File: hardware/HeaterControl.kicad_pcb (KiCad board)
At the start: 2 copper layers, 31.5 x 27.2 mm, 17 parts, among them J1 UART, J2 BTN, J3 OLED, P1 TC2030-CTX, Q1 NX7002AK.215, Q2 NX7002AK.215, SW1 RESET, U1 DS18B20, U2 BL654, U3 SHT30-DIS-B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

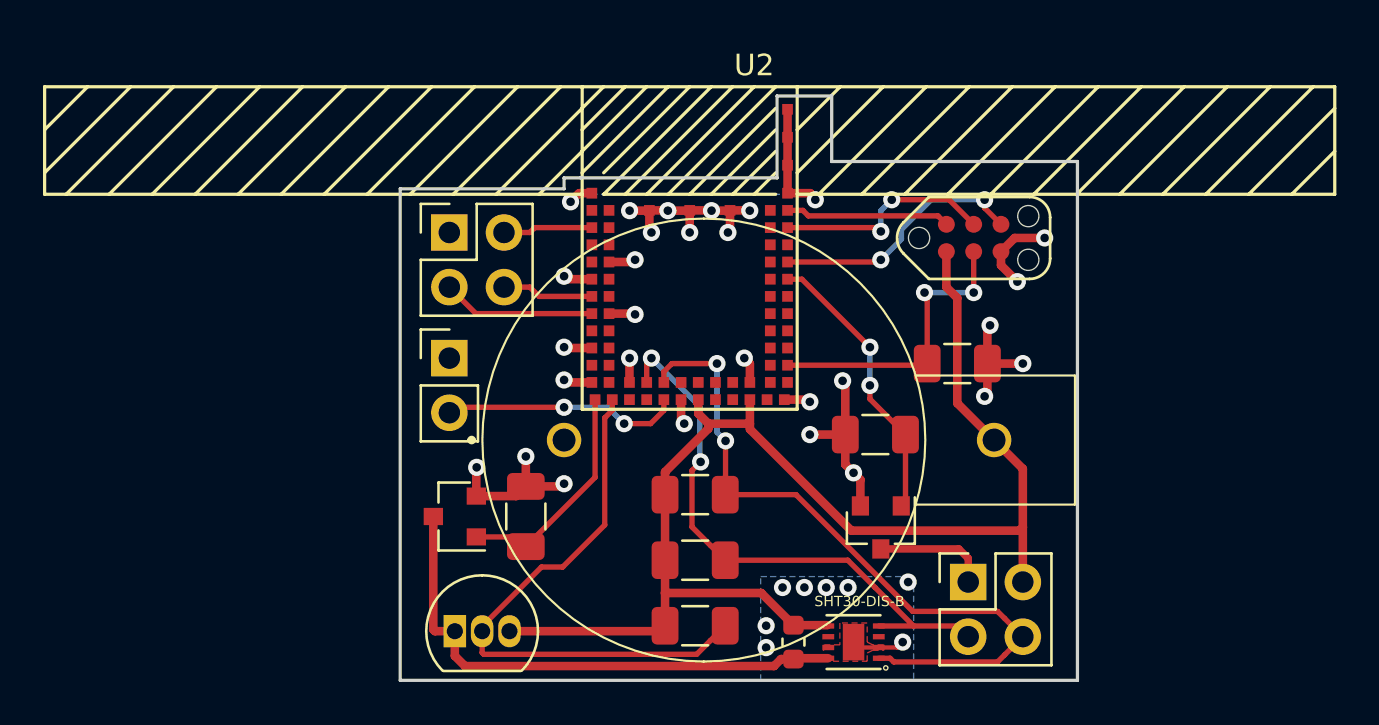
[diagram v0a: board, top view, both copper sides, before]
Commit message: Removed Sensor/Oled PWR circuts
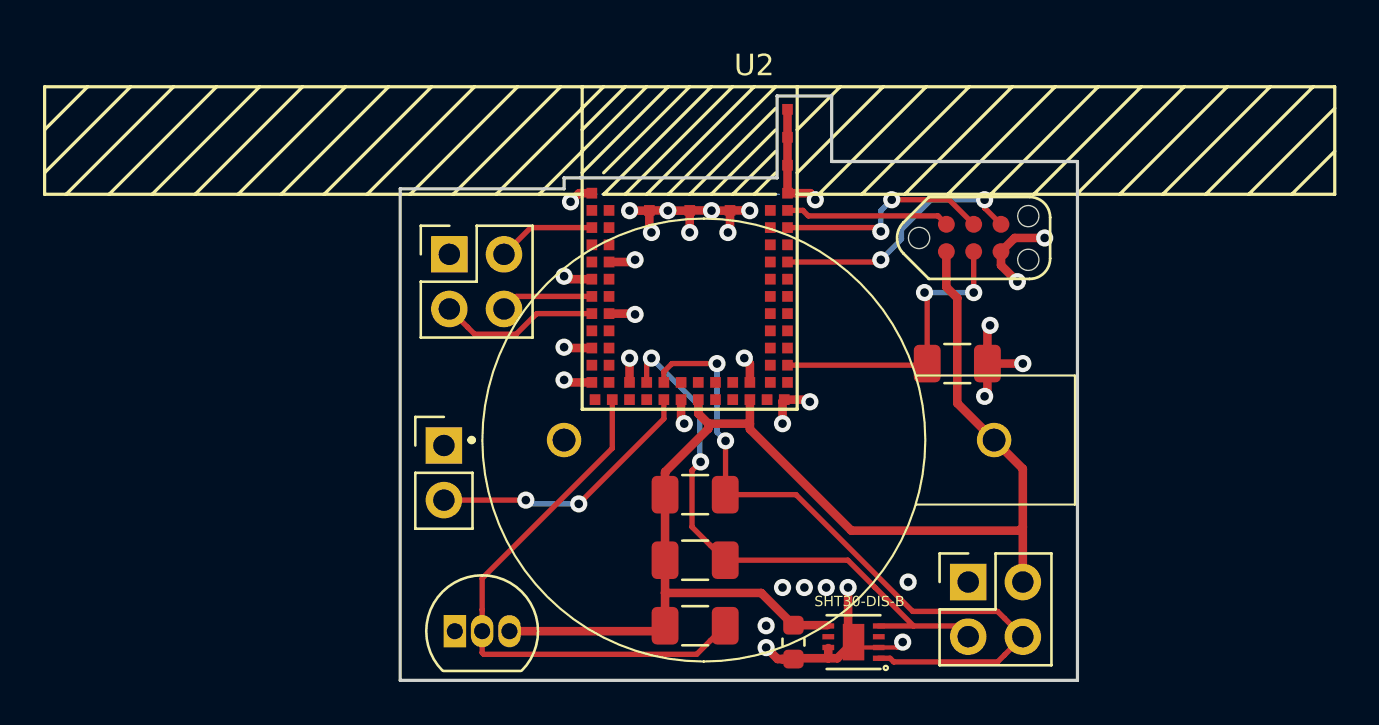
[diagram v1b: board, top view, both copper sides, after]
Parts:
- removed Q1, Q2: NX7002AK.215, Package_TO_SOT_SMD:SOT-23
- removed R3, R5: 100k, Resistor_SMD:R_1206_3216Metric
- moved J1 4.07 mm to (103.4, 79.8)
- moved J2 1.02 mm to (103.6, 70.9)
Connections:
- C1 pad 2: /SENSOR_GND -> GND
- J3 pad 1: /OLED_GND -> GND
- U1 pad 1: /SENSOR_GND -> GND
- U2 pad 42: /SENSOR_PWR -> Net-(U2-Pad42)
- U2 pad 9: /OLED_PWR -> Net-(U2-Pad9)
- U3 pad 2: /SENSOR_GND -> GND
- U3 pad 7: /SENSOR_GND -> GND
- U3 pad 8: /SENSOR_GND -> GND
- U3 pad 9: /SENSOR_GND -> GND
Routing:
- net /SENSOR_GND: track 27.6 -> 0.00 mm, vias 8 -> 0
- net /OLED_PWR: track 13.3 -> 0.00 mm, vias 2 -> 0
- net /SENSOR_PWR: track 10.7 -> 0.00 mm
- net /OLED_GND: track 5.35 -> 0.00 mm
- net GND: track 50.5 -> 47.0 mm, vias 29 -> 32
- net /UART_TX: track 11.2 -> 12.8 mm
- removed copper zone on B.Cu, net /SENSOR_GND
- removed copper zone on F.Cu, net /SENSOR_GND
